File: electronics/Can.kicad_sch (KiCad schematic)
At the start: 9 parts, among them J5 Conn_01x02_Socket, U3 MCP25625T-E/ML, Y2 8MHz

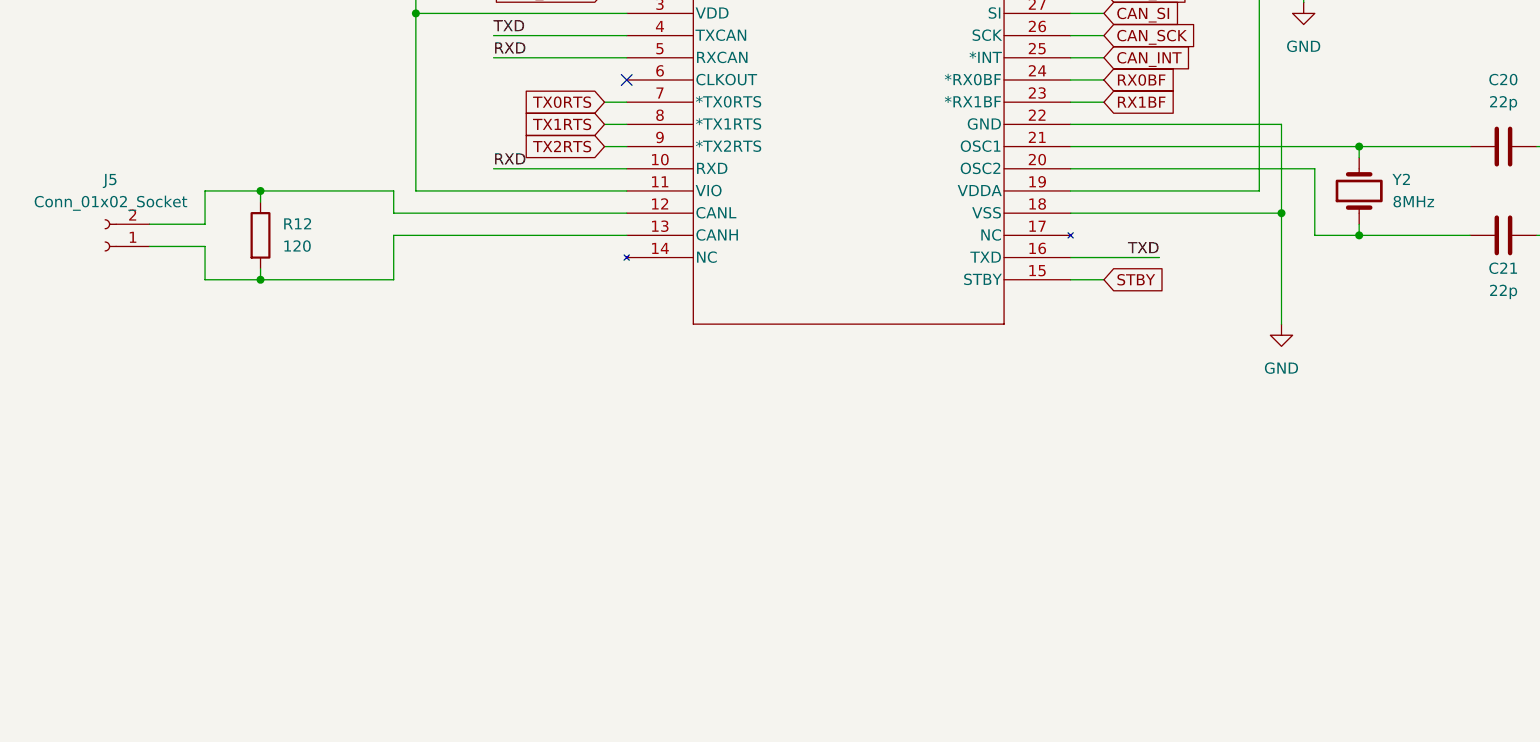
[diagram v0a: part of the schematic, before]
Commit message: Many changes to the design. Fully routed.
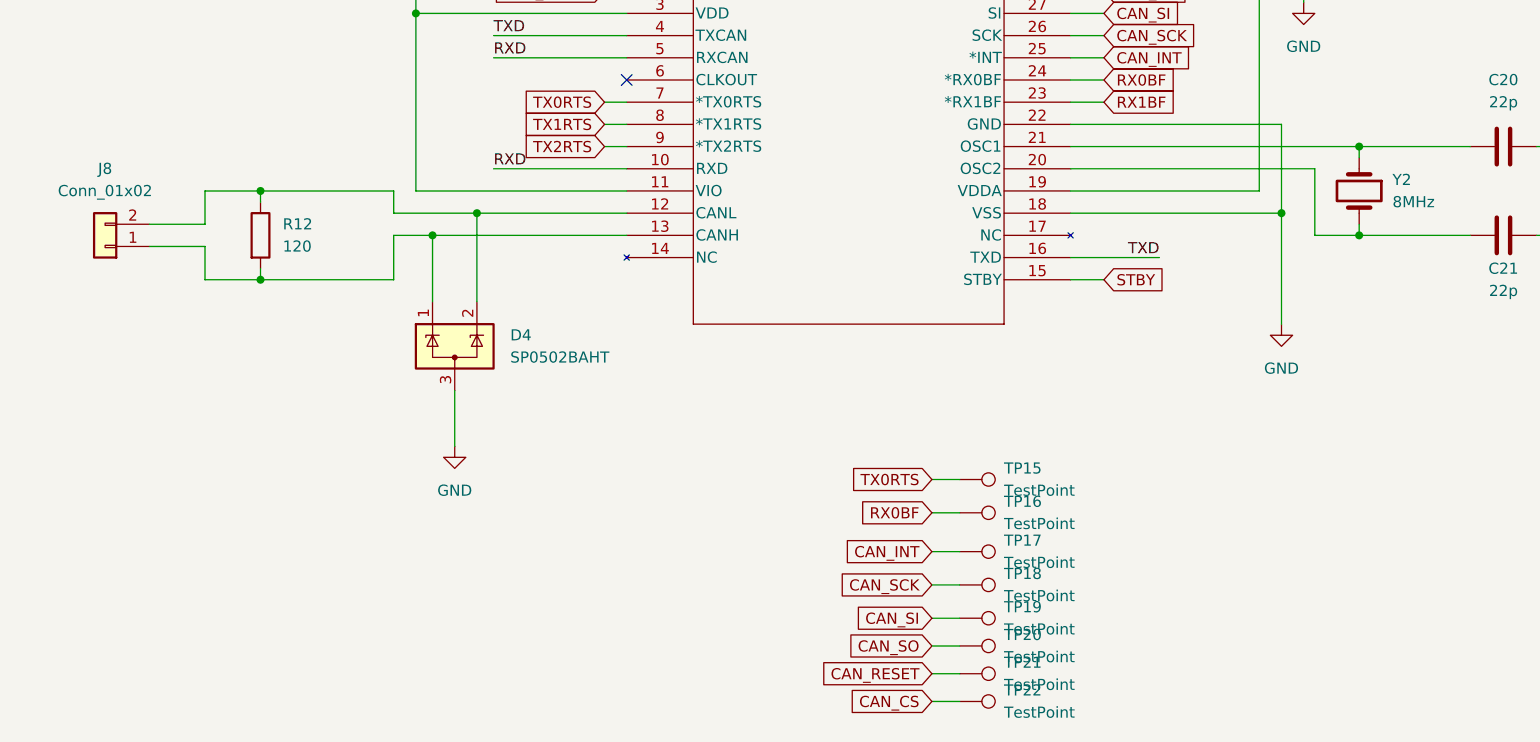
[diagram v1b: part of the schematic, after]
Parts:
- removed J5: Conn_01x02_Socket, Connector_JST:JST_EH_S2B-EH_1x02_P2.50mm_Horizontal, symbol Connector:Conn_01x02_Socket
- added D4: SP0502BAHT, Package_TO_SOT_SMD:SOT-23, symbol Power_Protection:SP0502BAHT
- added J8: Conn_01x02, Connector_Phoenix_MSTB:PhoenixContact_MSTBVA_2,5_2-G_1x02_P5.00mm_Vertical, symbol Connector_Generic:Conn_01x02
- added TP15, TP16, TP17, TP18, TP19, TP20, TP21, TP22: TestPoint, TestPoint:TestPoint_Pad_D1.0mm, symbol Connector:TestPoint
- C17, C18, C19, C20, C21: footprint Capacitor_SMD:C_0603_1608Metric_Pad1.08x0.95mm_HandSolder -> Capacitor_SMD:C_0402_1005Metric
- R12: footprint Resistor_SMD:R_0603_1608Metric_Pad0.98x0.95mm_HandSolder -> Resistor_SMD:R_0402_1005Metric
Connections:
- net CAN_CS: now also TP22.1
- net CAN_INT: now also TP17.1
- net CAN_RESET: now also TP21.1
- net CAN_SCK: now also TP18.1
- net CAN_SI: now also TP19.1
- net CAN_SO: now also TP20.1
- net GND: now also D4.3 (A)
- net RX0BF: now also TP16.1
- net TX0RTS: now also TP15.1
- net at C20.1, U3.21 (OSC1): now also Y2.1; no longer Y2.2
- net at C21.1, U3.20 (OSC2): now also Y2.2; no longer Y2.1
- net at R12.1, U3.12 (CANL): now also D4.2 (K), J8.2 (Pin_2)
- net at R12.2, U3.13 (CANH): now also D4.1 (K), J8.1 (Pin_1)
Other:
- moved on the sheet: Y2

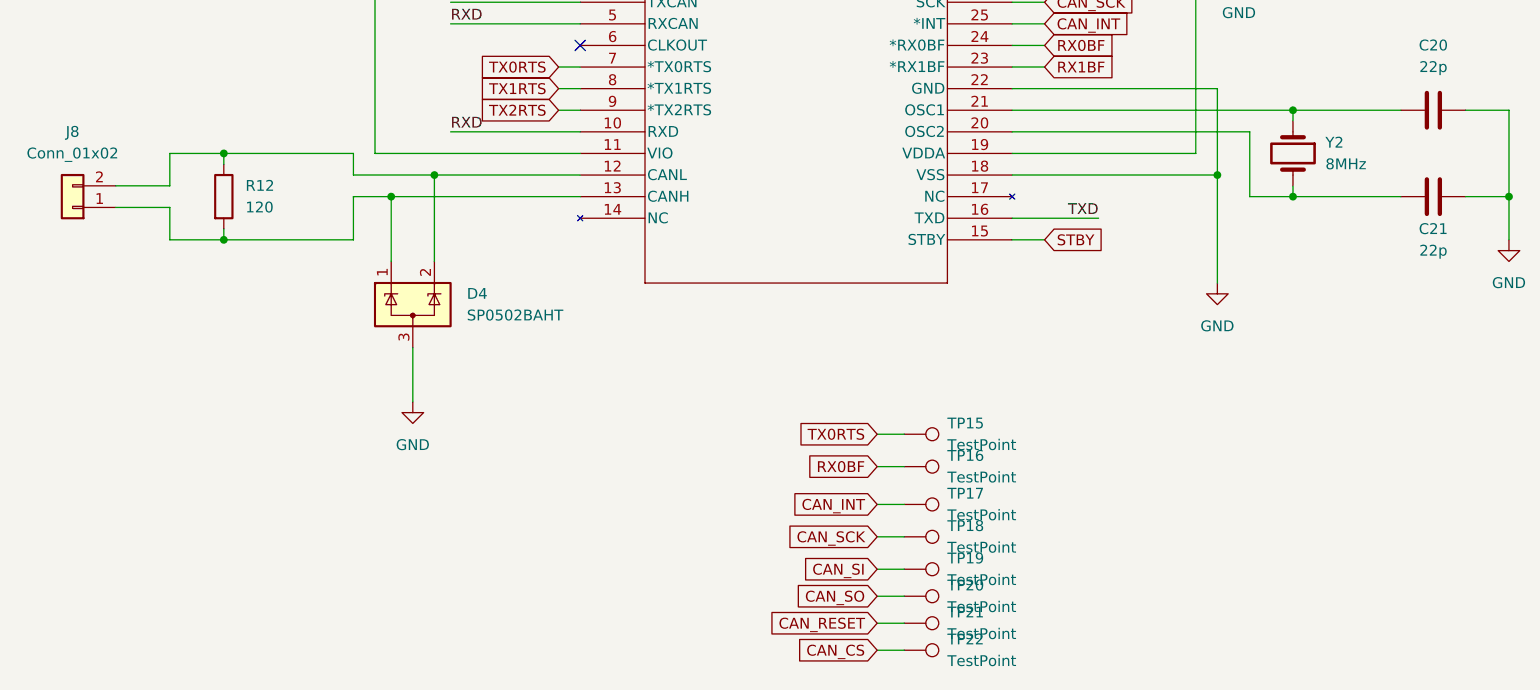
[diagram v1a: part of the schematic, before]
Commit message: Almost sent this to fab. It is getting expensive.
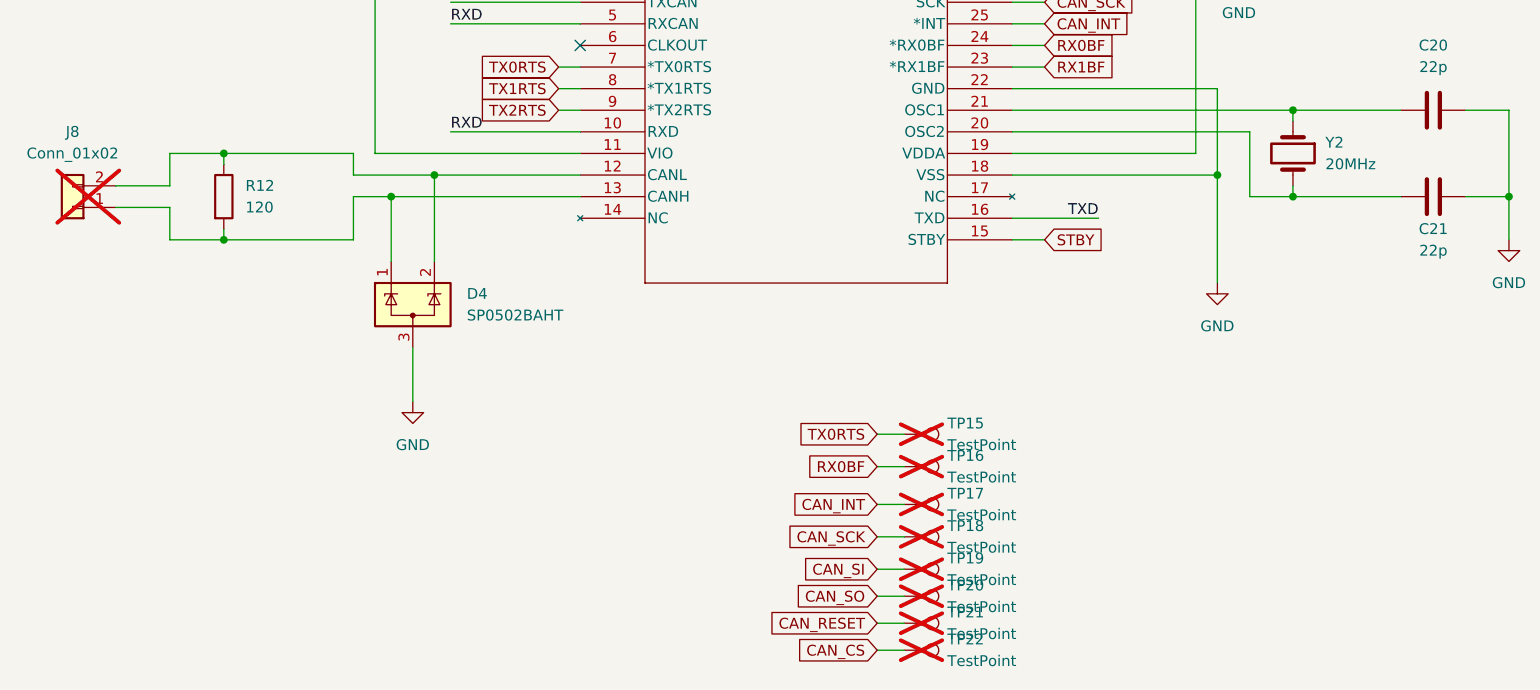
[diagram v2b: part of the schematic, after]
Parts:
- C17, C18, C19: JLCPCB (none) -> C2655418
- D4: JLCPCB (none) -> C207261
- J8, TP15, TP16, TP17, TP18, TP19, TP20, TP21, TP22: now not fitted
- Y2: value 8MHz -> 20MHz; JLCPCB C403948 -> C2901674

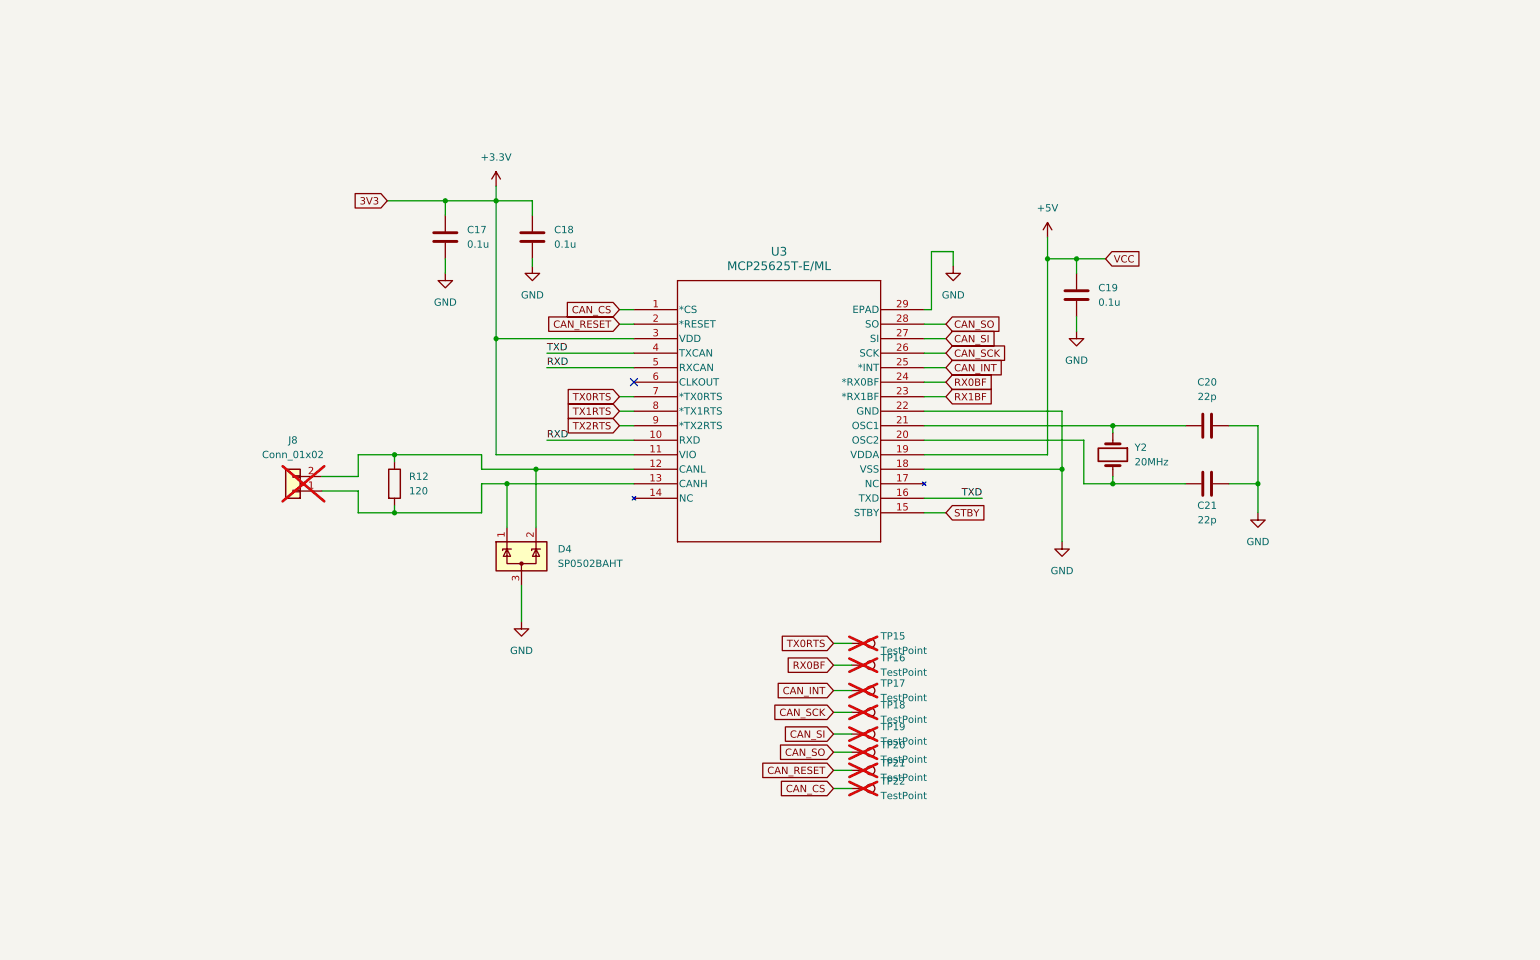
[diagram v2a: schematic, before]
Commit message: Switched processor.
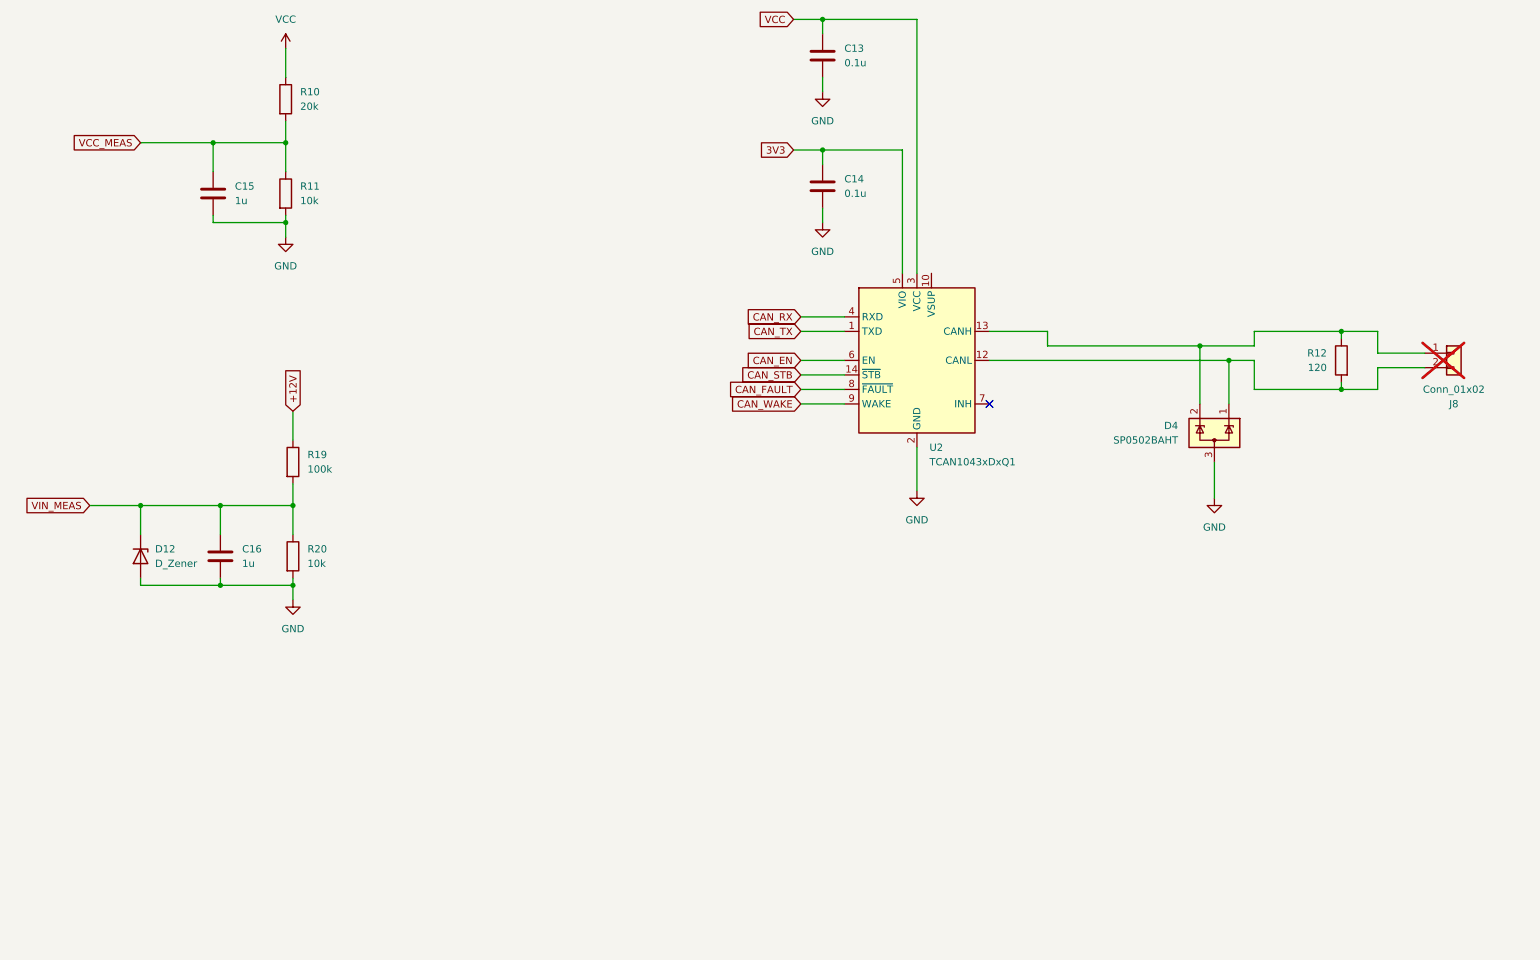
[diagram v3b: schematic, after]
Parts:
- removed C17, C18, C19: 0.1u, Capacitor_SMD:C_0402_1005Metric, symbol Device:C
- removed C20, C21: 22p, Capacitor_SMD:C_0402_1005Metric, symbol Device:C
- removed TP15, TP16, TP17, TP18, TP19, TP20, TP21, TP22: TestPoint, TestPoint:TestPoint_Pad_D1.0mm, symbol Connector:TestPoint
- removed U3: MCP25625T-E/ML, Package_DFN_QFN:QFN-28-1EP_6x6mm_P0.65mm_EP4.25x4.25mm, symbol General:MCP25625T-E_ML
- removed Y2: 20MHz, Crystal:Crystal_SMD_3225-4Pin_3.2x2.5mm, symbol Device:Crystal
- added C13, C14: 0.1u, Capacitor_SMD:C_0402_1005Metric, symbol Device:C
- added C15, C16: 1u, Capacitor_SMD:C_0402_1005Metric, symbol Device:C
- added D12: D_Zener, Diode_SMD:D_SOD-123, symbol Device:D_Zener
- added R10: 20k, Resistor_SMD:R_0402_1005Metric, symbol Device:R
- added R11, R20: 10k, Resistor_SMD:R_0402_1005Metric, symbol Device:R
- added R19: 100k, Resistor_SMD:R_0402_1005Metric, symbol Device:R
- added U2: TCAN1043xDxQ1, Package_SO:SOIC-14_3.9x8.7mm_P1.27mm, symbol Interface_CAN_LIN:TCAN1043xDxQ1
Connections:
- net GND: now also C13.2, C14.2, C15.2, C16.2, D12.2 (A), R11.2, R20.2, U2.2 (GND)
- net at D4.1 (K), R12.2: now also J8.2 (Pin_2), U2.12 (CANL); no longer J8.1 (Pin_1)
- net at D4.2 (K), R12.1: now also J8.1 (Pin_1), U2.13 (CANH); no longer J8.2 (Pin_2)
- new net +12V: R19.1
- new net 3V3: C14.1, U2.5 (VIO)
- new net CAN_EN: U2.6 (EN)
- new net CAN_FAULT: U2.8 (~{FAULT})
- new net CAN_RX: U2.4 (RXD)
- new net CAN_STB: U2.14 (~{STB})
- new net CAN_TX: U2.1 (TXD)
- new net CAN_WAKE: U2.9 (WAKE)
- new net VCC: C13.1, R10.1, U2.3 (VCC)
- new net VCC_MEAS: C15.1, R10.2, R11.1
- new net VIN_MEAS: C16.1, D12.1 (K), R19.2, R20.1
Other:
- moved on the sheet: D4, J8, R12

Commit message: Ordered this version.
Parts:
- C13, C14: JLCPCB C2655418 -> C432917
- R11, R20: JLCPCB (none) -> C100572
- R12: JLCPCB (none) -> C258113
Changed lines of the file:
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@@
+			)
+		)
+		(property "JLCPCB" "C100572"
+			(at 69.85 119.38 0)
+			(effects
+				(font
+					(size 1.27 1.27)
+				)
+				(hide yes)
 			)
 		)
@@
 			)
 		)
-		(property "JLCPCB" "C2655418 "
+		(property "JLCPCB" "C432917"
 			(at 162.56 31.75 0)
 			(effects
@@
 			)
 		)
+		(property "JLCPCB" "C258113"
+			(at 253.365 85.09 0)
+			(effects
+				(font
+					(size 1.27 1.27)
+				)
+				(hide yes)
+			)
+		)
 		(pin "1"
 		)
@@
 			)
 		)
+		(property "JLCPCB" "C100572"
+			(at 68.58 55.88 0)
+			(effects
+				(font
+					(size 1.27 1.27)
+				)
+				(hide yes)
+			)
+		)
 		(pin "2"
 		)
@@
 			)
 		)
-		(property "JLCPCB" "C2655418 "
+		(property "JLCPCB" "C432917"
 			(at 162.56 54.61 0)
 			(effects

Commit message: Tweaked parts to use Basic parts which are cheaper.
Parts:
- C13, C14: JLCPCB C432917 -> C1525
- D4: JLCPCB C207261 -> C32677
- R11, R20: JLCPCB C100572 -> C25744
- R12: footprint Resistor_SMD:R_0402_1005Metric -> Resistor_SMD:R_0603_1608Metric; JLCPCB C258113 -> C22787
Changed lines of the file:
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@@
 			)
 		)
-		(property "JLCPCB" "C100572"
+		(property "JLCPCB" "C25744"
 			(at 69.85 119.38 0)
 			(effects
@@
 			)
 		)
-		(property "JLCPCB" "C432917"
+		(property "JLCPCB" "C1525"
 			(at 162.56 31.75 0)
 			(effects
@@
 			)
 		)
-		(property "Footprint" "Resistor_SMD:R_0402_1005Metric"
+		(property "Footprint" "Resistor_SMD:R_0603_1608Metric"
 			(at 255.143 85.09 90)
 			(effects
@@
 			)
 		)
-		(property "JLCPCB" "C258113"
+		(property "JLCPCB" "C22787"
 			(at 253.365 85.09 0)
 			(effects
@@
 			)
 		)
-		(property "JLCPCB" "C207261"
+		(property "JLCPCB" "C32677"
 			(at 231.14 97.79 0)
 			(effects
@@
 			)
 		)
-		(property "JLCPCB" "C100572"
+		(property "JLCPCB" "C25744"
 			(at 68.58 55.88 0)
 			(effects
@@
 			)
 		)
-		(property "JLCPCB" "C432917"
+		(property "JLCPCB" "C1525"
 			(at 162.56 54.61 0)
 			(effects

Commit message: Updated design for REV B.
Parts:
- removed J8: Conn_01x02, Connector_Phoenix_MSTB:PhoenixContact_MSTBVA_2,5_2-G_1x02_P5.00mm_Vertical, symbol Connector_Generic:Conn_01x02
- added H1: MountingHole, footprints:brushless_buddy_logo, symbol Mechanical:MountingHole
- added J10: Conn_01x04, Connector_JST:JST_PH_S4B-PH-K_1x04_P2.00mm_Horizontal, symbol Connector_Generic:Conn_01x04
- R10: JLCPCB (none) -> C93942
- R19: JLCPCB (none) -> C102750
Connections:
- net VCC: now also U2.10 (VSUP)
- net at D4.1 (K), R12.2, U2.12 (CANL): now also J10.2 (Pin_2), J10.4 (Pin_4)
- net at D4.2 (K), R12.1, U2.13 (CANH): now also J10.1 (Pin_1), J10.3 (Pin_3)
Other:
- moved on the sheet: D4, R12

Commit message: This version is working well. Need to figure out USB DFU programming.
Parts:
- C15, C16: JLCPCB (none) -> C52923
- J10: Digikey 455-B4B-PH-SM4-TBCT-ND -> 455-1721-ND
- R12: footprint Resistor_SMD:R_0603_1608Metric -> Resistor_SMD:R_0402_1005Metric; JLCPCB C22787 -> C25079
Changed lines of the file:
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@@
+			)
+		)
+		(property "JLCPCB" "C52923"
+			(at 55.88 55.88 0)
+			(effects
+				(font
+					(size 1.27 1.27)
+				)
+				(hide yes)
 			)
 		)
@@
 		)
 		(property "Description" ""
+			(at 57.15 119.38 0)
+			(effects
+				(font
+					(size 1.27 1.27)
+				)
+				(hide yes)
+			)
+		)
+		(property "JLCPCB" "C52923"
 			(at 57.15 119.38 0)
 			(effects
@@
 			)
 		)
-		(property "Footprint" "Resistor_SMD:R_0603_1608Metric"
+		(property "Footprint" "Resistor_SMD:R_0402_1005Metric"
 			(at 241.173 83.82 90)
 			(effects
@@
 			)
 		)
-		(property "JLCPCB" "C22787"
+		(property "JLCPCB" "C25079"
 			(at 239.395 83.82 0)
 			(effects
@@
 			)
 		)
-		(property "Digikey" "455-B4B-PH-SM4-TBCT-ND"
+		(property "Digikey" "455-1721-ND"
 			(at 270.51 85.09 0)
 			(effects
